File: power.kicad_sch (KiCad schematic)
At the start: 30 parts, among them J5 Molex_Nano-Fit_1x2_105309-1202, Q1 AO3401A, SW1 SW_EG1218, U4 AP62301_TSOT, U6 MCP1700T-3302E_TT

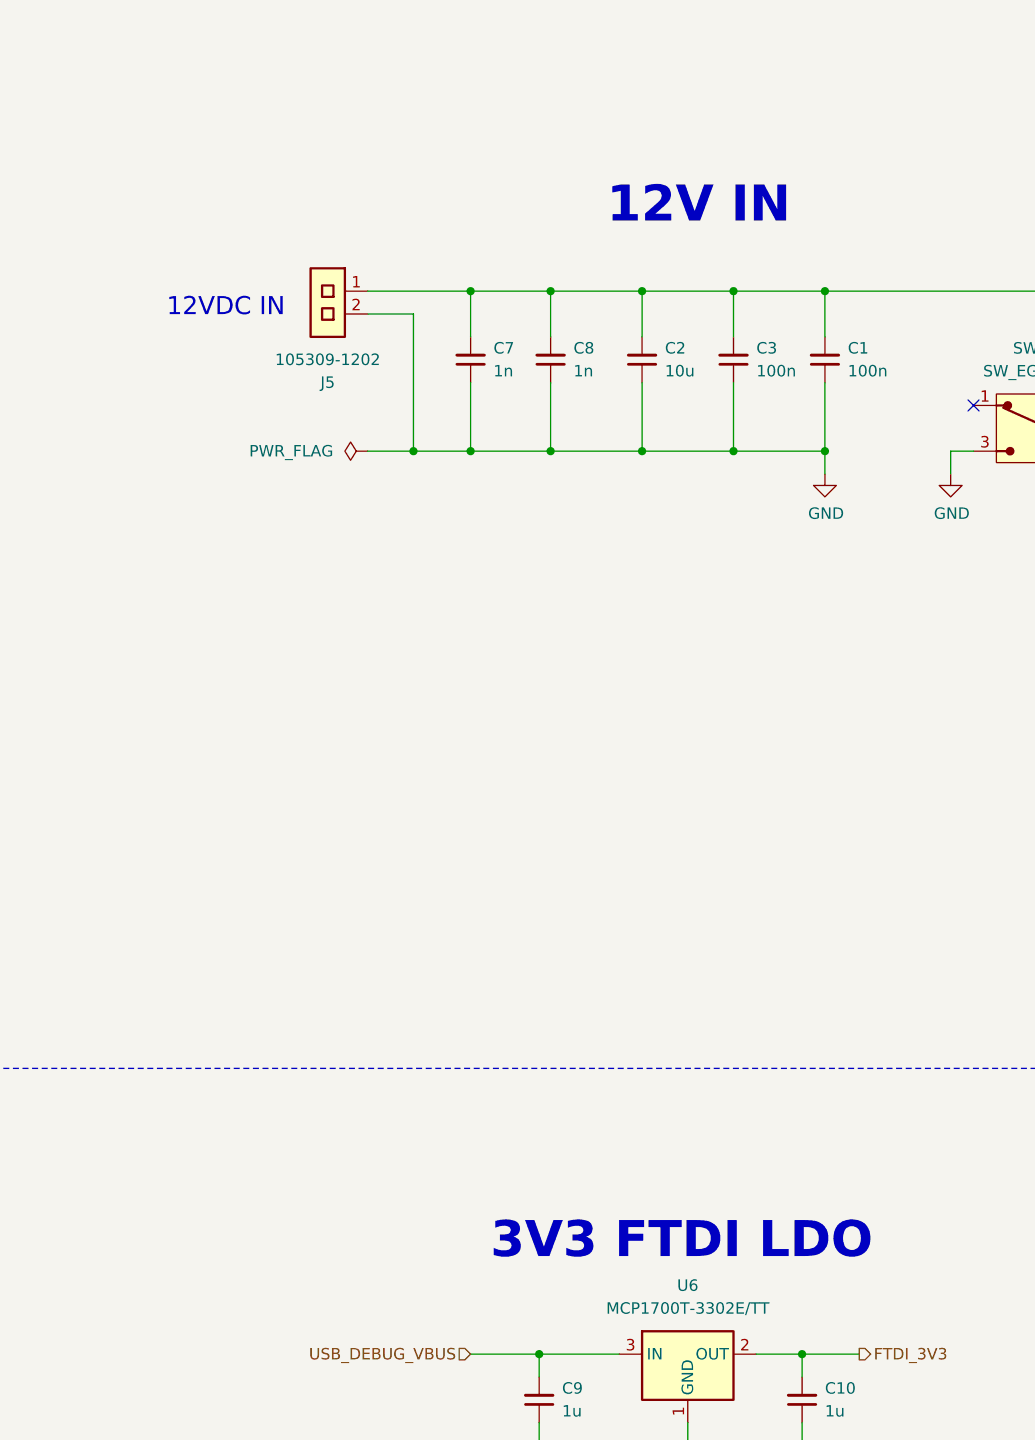
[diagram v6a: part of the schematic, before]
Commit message: [#93514] Align items to grid, add NC-SI testpads
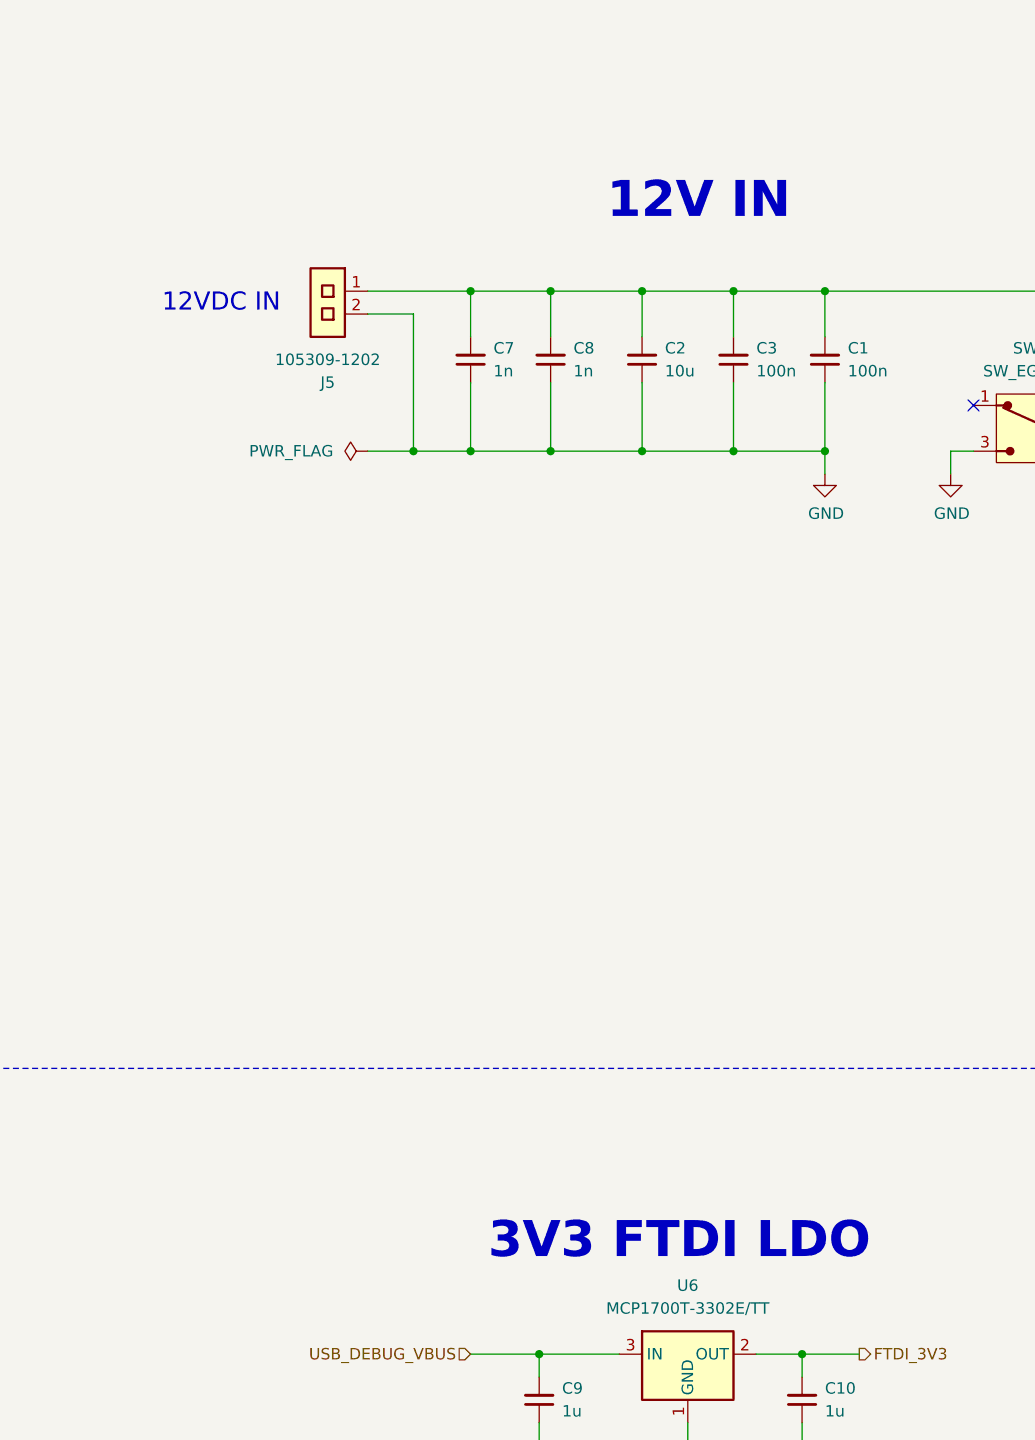
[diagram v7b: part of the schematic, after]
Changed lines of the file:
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@@
 	(text "12VDC IN"
 		(exclude_from_sim no)
-		(at 50.038 76.708 0)
+		(at 49.53 76.2 0)
 		(effects
 			(font
@@
 	(text "3V3 FTDI LDO"
 		(exclude_from_sim no)
-		(at 128.524 181.61 0)
+		(at 128.27 181.61 0)
 		(effects
 			(font
@@
 	(text "12V IN"
 		(exclude_from_sim no)
-		(at 119.38 66.548 0)
+		(at 119.38 66.04 0)
 		(effects
 			(font
